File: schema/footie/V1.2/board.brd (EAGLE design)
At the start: 69.5 x 53.3 mm, 41 parts, among them T1 2N3565, U2 USD-SOCKETNEW, U3 HC_05, U4 MCP73831, U5 3.3 regulator, U6 ATMEGA328P-AU

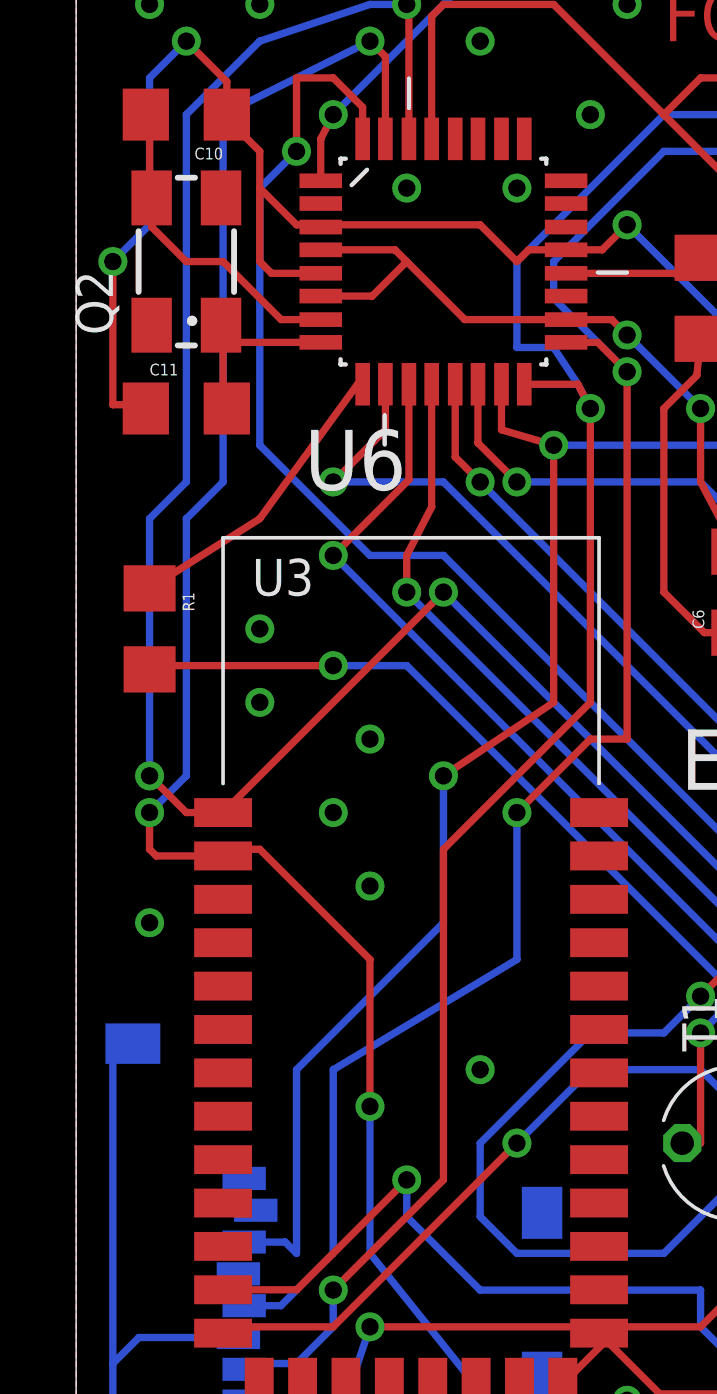
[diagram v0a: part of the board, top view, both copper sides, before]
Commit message: fix missing wire
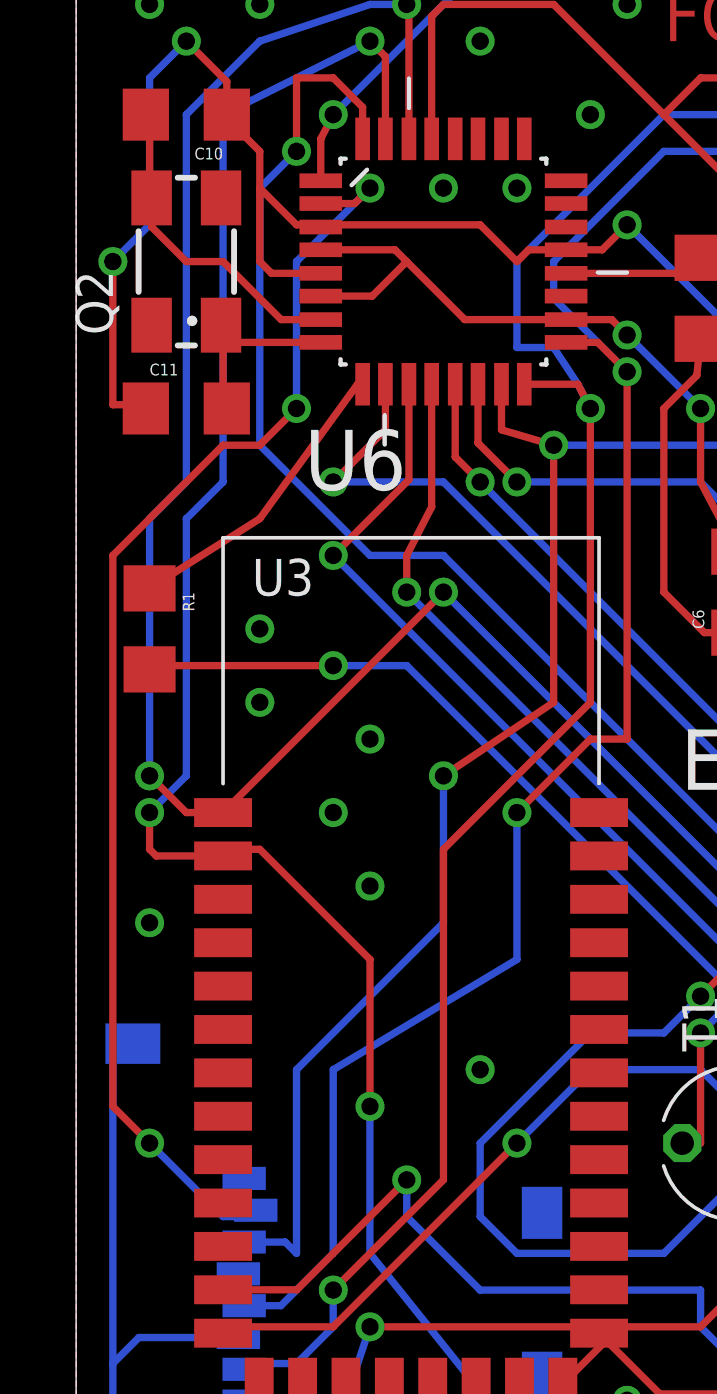
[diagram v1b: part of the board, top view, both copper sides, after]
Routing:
- net SD_CS: track 0.00 -> 45.0 mm, vias 0 -> 3
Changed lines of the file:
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@@
 <?xml version="1.0" encoding="utf-8"?>
 <!DOCTYPE eagle SYSTEM "eagle.dtd">
-<eagle version="7.3.0">
+<eagle version="7.4.0">
 <drawing>
 <settings>
@@
 <grid distance="0.05" unitdist="inch" unit="mm" style="lines" multiple="1" display="no" altdistance="0.025" altunitdist="inch" altunit="mm"/>
 <layers>
-<layer number="1" name="Top" color="4" fill="1" visible="no" active="yes"/>
+<layer number="1" name="Top" color="4" fill="1" visible="yes" active="yes"/>
 <layer number="16" name="Bottom" color="1" fill="1" visible="yes" active="yes"/>
 <layer number="17" name="Pads" color="2" fill="1" visible="yes" active="yes"/>
@@
 <contactref element="U6" pad="2"/>
 <contactref element="U2" pad="2"/>
-<wire x1="6.21" y1="9.11" x2="8.4582" y2="43.9166" width="0" layer="19" extent="1-16"/>
+<wire x1="8.4582" y1="43.9166" x2="9.6266" y2="43.9166" width="0.254" layer="1"/>
+<wire x1="9.6266" y1="43.9166" x2="10.16" y2="44.45" width="0.254" layer="1"/>
+<via x="10.16" y="44.45" extent="1-16" drill="0.6"/>
+<wire x1="5.08" y1="8.89" x2="6.35" y2="8.89" width="0.254" layer="16"/>
+<wire x1="2.54" y1="11.43" x2="5.08" y2="8.89" width="0.254" layer="16"/>
+<wire x1="1.27" y1="12.7" x2="2.54" y2="11.43" width="0.254" layer="1"/>
+<wire x1="1.27" y1="31.75" x2="1.27" y2="12.7" width="0.254" layer="1"/>
+<wire x1="5.08" y1="35.56" x2="1.27" y2="31.75" width="0.254" layer="1"/>
+<wire x1="6.35" y1="35.56" x2="5.08" y2="35.56" width="0.254" layer="1"/>
+<wire x1="7.62" y1="36.83" x2="6.35" y2="35.56" width="0.254" layer="1"/>
+<wire x1="7.62" y1="41.91" x2="7.62" y2="36.83" width="0.254" layer="16"/>
+<wire x1="10.16" y1="44.45" x2="7.62" y2="41.91" width="0.254" layer="16"/>
+<wire x1="6.35" y1="8.89" x2="6.21" y2="9.11" width="0.254" layer="16"/>
+<via x="2.54" y="11.43" extent="1-16" drill="0.6"/>
+<via x="7.62" y="36.83" extent="1-16" drill="0.6"/>
 </signal>
 <signal name="SD_SCK">
@@
 <via x="2.54" y="19.05" extent="1-16" drill="0.6"/>
 <via x="13.97" y="13.97" extent="1-16" drill="0.6"/>
-<via x="11.43" y="44.45" extent="1-16" drill="0.6"/>
+<via x="12.7" y="44.45" extent="1-16" drill="0.6"/>
 <via x="15.24" y="44.45" extent="1-16" drill="0.6"/>
 <via x="19.05" y="2.54" extent="1-16" drill="0.6"/>
